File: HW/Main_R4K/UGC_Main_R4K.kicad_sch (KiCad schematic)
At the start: 165 parts, among them J1 SM02B-SURS-TF_LF__SN_, J10 SM02B-SURS-TF_LF__SN_, J13 503480-0640, J2 503480-0640, J4 Conn_01x06_Pin, J5 UJ31-CH-G1-SMT-TR, J6 Trigger, J7 Trigger, J8 Conn_01x02, J9 Conn_01x02, Q1 MMBT3904, Q2 MMBT3904, Q3 BSS138DW, Q4 BSS138DW, Q5 MMBT2222A, Q6 MMBT2222A, SW1 1TS026A-1000-0550, SW1 SW_Push, SW10 SW_Push, SW11 SW_Push, SW12 SW_Push, SW13 SW_Push, SW14 SW_TS-1187A, SW17 SW_TS-1187A, SW18 SW_TS-1187A, SW19 SW_TS-1187A, SW2 SW_Push, SW3 SW_Push, SW4 SW_Push, SW5 SW_TS-1187A, SW6 GL18_SW, SW7 SW_Push, SW8 SW_Push, SW9 SW_TS-1187A, U1 ESP32-PICO-MINI-02, U10 ST_LSM6, U11 BQ25180, U12 CH340K, U13 PI3USB4000A, U2 GD25Q80EEIGR, U4 TPS630001RCR, U5 ST_LSM6, U6 MCP3002, U7 MCP3002, U8 RP2040, X1 ModConnect, X2 ModConnect, X3 ModConnect, X4 ModConnect, X5 ModConnect, X6 ModConnect, Y1 Crystal_GND3

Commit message: Update PCB schematic
 fix diode issue
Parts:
- D14, D15, D16, D3, D6, D7: MPN B5819W SL -> B5819WT
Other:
- note added: "3.3 Regulation"
- note added: "Analog Joystick"
- note added: "I/O Buttons"
- note added: "USB I/O"
- company: (none) -> Hand Held Legend, LLC
- moved on the sheet: B1, C1, C10, C12, C13, C14, C15, C16, C17, C18, C2, C20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

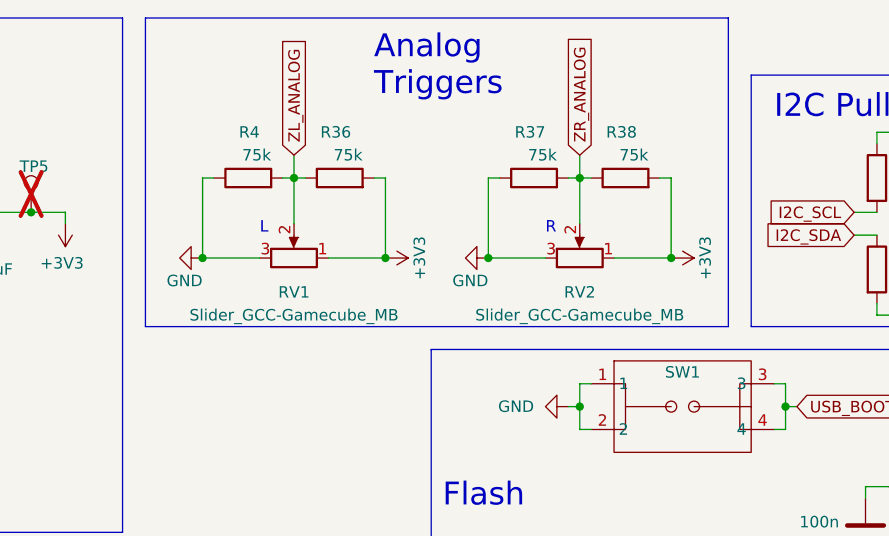
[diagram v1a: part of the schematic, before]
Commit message: Update CAD files
- PCB uses a new socket type for the slider potentiometers
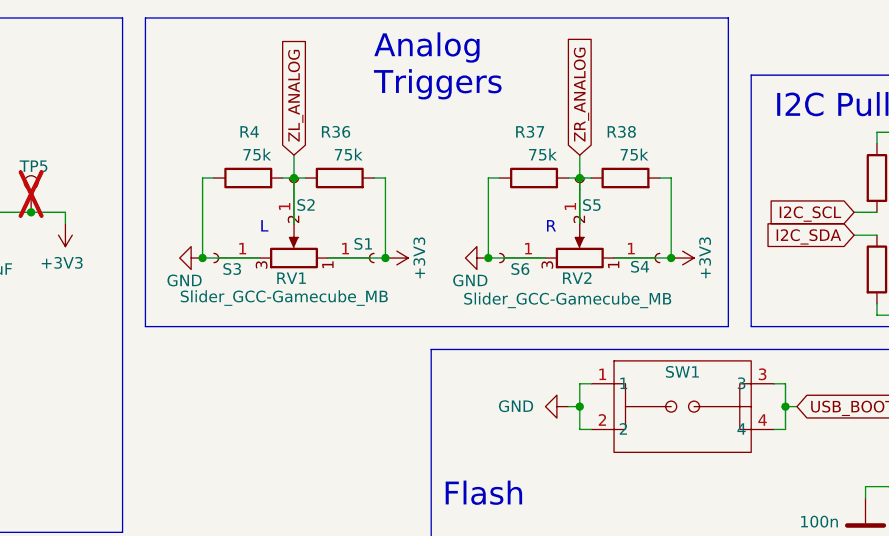
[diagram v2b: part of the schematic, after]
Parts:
- added S1, S2, S3, S4, S5, S6: 4015-0-43-80-30-27-10-0, hhl:4015-0-43-80-30-27-10-0, symbol Connector:Conn_01x01_Socket
- RV1, RV2: footprint hhl:GCC_Slider_MillMax -> hhl:GCC_Slider_MillMaxSocketed; symbol hhl:Slider_GCC-Gamecube_MillMax_MB -> hhl:Slider_GCC-Gamecube_SolderInsert
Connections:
- net +3V3: now also S1.1 (Pin_1), S4.1 (Pin_1); no longer RV1.1 (GND), RV2.1 (GND)
- net GND: now also S3.1 (Pin_1), S6.1 (Pin_1); no longer RV1.3 (V+), RV2.3 (V+)
- net ZL_ANALOG: now also S2.1 (Pin_1); no longer RV1.2 (Signal)
- net ZR_ANALOG: now also S5.1 (Pin_1); no longer RV2.2 (Signal)

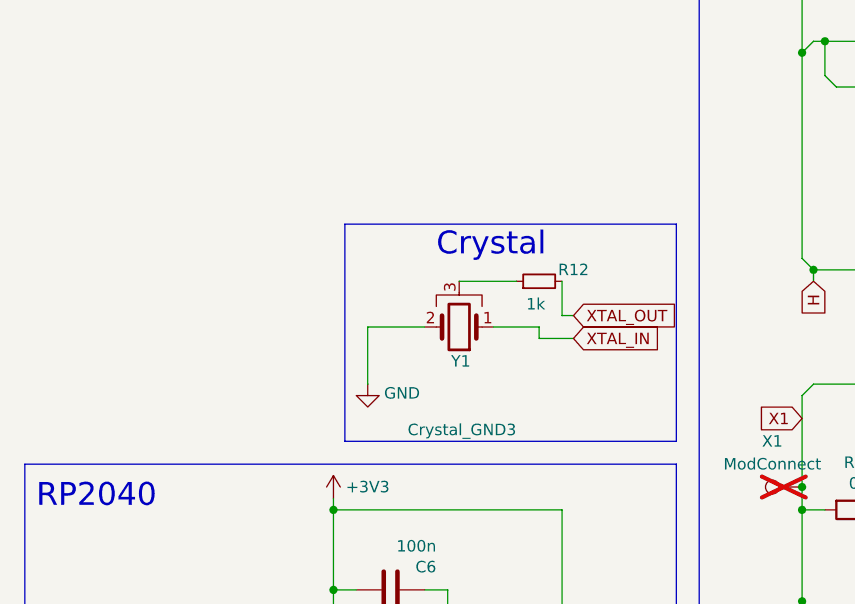
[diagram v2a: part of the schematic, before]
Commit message: Update PCBs
- New S1 variant
- Update crystal and socket mounts for trigger sliders
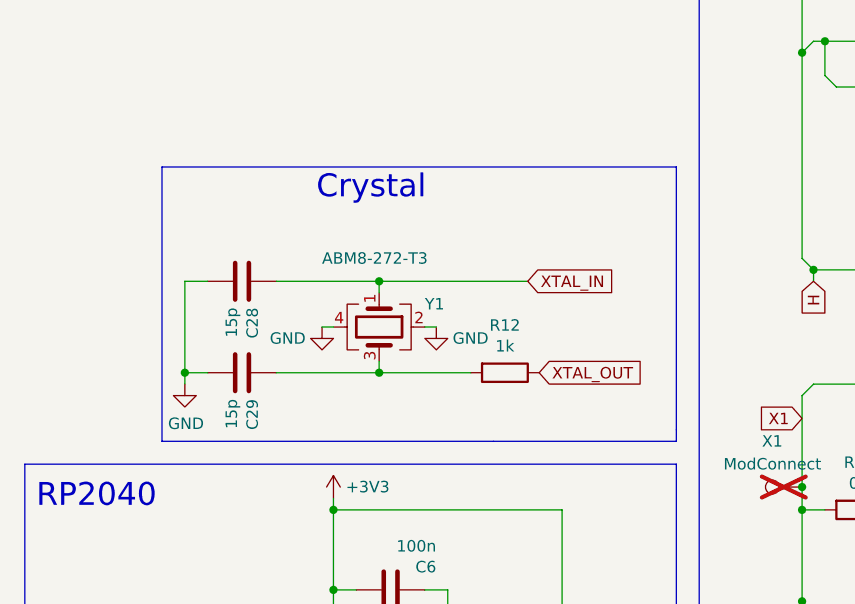
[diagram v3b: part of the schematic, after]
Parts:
- removed R12: 1k, Resistor_SMD:R_0201_0603Metric, symbol Device:R_Small
- removed Y1: Crystal_GND3, Crystal:Resonator_SMD_Murata_CSTxExxV-3Pin_3.0x1.1mm, symbol Device:Crystal_GND3
- added C28, C29: 15p, Capacitor_SMD:C_0402_1005Metric, symbol Device:C
- added R12: 1k, Resistor_SMD:R_0402_1005Metric, symbol Device:R
- added Y1: ABM8-272-T3, Crystal:Crystal_SMD_3225-4Pin_3.2x2.5mm, symbol Device:Crystal_GND24
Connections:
- net GND: now also C28.2, C29.2, Y1.2, Y1.4
- net XTAL_IN: now also C28.1, Y1.1
- net XTAL_OUT: now also R12.1
- new net: C29.1, R12.2, Y1.3

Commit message: Update PCBs
- Fix BOMs so they reference real part numbers
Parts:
- removed N1, N2, N3, N4, N5, N6: 0630-0-15-15-30-27-10-0, N/A, symbol Connector_Generic:Conn_01x01
- B1, J6, J7: LCSC (none) -> C7499302; MPN (none) -> PH2.0 mm Female; Price (none) -> 0.0098
- C1: value 47uF 6.3v -> 47uF; LCSC (none) -> C7190; MPN (none) -> TAJA476K006RNJ; Price (none) -> 0.0544
- C1, C2: value .047u -> 47nF; footprint Capacitor_SMD:C_0603_1608Metric_Pad1.08x0.95mm_HandSolder -> Capacitor_SMD:C_0603_1608Metric; LCSC C15849 -> C519554; MPN (none) -> CC0603JRX7R9BB473; Price (none) -> 0.0026
- C10, C15, C18, C20, C22, C24, C6: value 100n -> 100nF; LCSC (none) -> C160831; MPN (none) -> CL03A104KQ3NNNC; Price (none) -> 0.0007
- C10, C5, C7, C9: value 100n -> 100nF; footprint Capacitor_SMD:C_0402_1005Metric -> Capacitor_SMD:C_0201_0603Metric; LCSC (none) -> C160831; MPN (none) -> CL03A104KQ3NNNC; Price (none) -> 0.0007
- C12, C13: footprint Capacitor_SMD:C_0603_1608Metric -> Capacitor_SMD:C_0201_0603Metric; LCSC C1525 -> C160831; MPN (none) -> CL03A104KQ3NNNC; Price (none) -> 0.0007
- C14, C16, C21, C26, C27, C33, C34: value 1u -> 1uF; LCSC (none) -> C76929; MPN (none) -> GRM033R60J105KEA2D; Price (none) -> 0.0015
- C17: footprint Capacitor_SMD:C_0402_1005Metric -> Capacitor_SMD:C_0805_2012Metric; LCSC (none) -> C17024; MPN (none) -> CL21A106KPFNNNE; Price (none) -> 0.0050
- C2, C3: LCSC (none) -> C17024; MPN (none) -> CL21A106KPFNNNE; Price (none) -> 0.0050
- C2: value 10uF/10V (20%) -> 10uF; footprint Capacitor_SMD:C_0603_1608Metric -> Capacitor_SMD:C_0805_2012Metric; LCSC (none) -> C17024; MPN (none) -> CL21A106KPFNNNE; Price (none) -> 0.0050
- C25, C32: LCSC (none) -> C160831; MPN (none) -> CL03A104KQ3NNNC; Price (none) -> 0.0007
- C28, C29: value 15p -> 15pF; LCSC (none) -> C85891; MPN (none) -> GRM0335C1H150JA01D; Price (none) -> 0.0011
- C8: value 1u -> 1uF; footprint Capacitor_SMD:C_0402_1005Metric -> Capacitor_SMD:C_0201_0603Metric; LCSC (none) -> C76929; MPN (none) -> GRM033R60J105KEA2D; Price (none) -> 0.0015
- D1, D10, D9: LCSC (none) -> C27636112; Price 0.0449 -> 0.0092
- D1, D11, D12, D13, D2, D8: LCSC (none) -> C135826; MPN (none) -> BAS16VY,115
- J1, J10: LCSC (none) -> C566239
- J13, J2: LCSC (none) -> C3168077
- J4, J8, J9, JP1, SW1, SW10, SW11, SW12, SW13, SW2, SW3, SW4, TP1, TP2, TP5, TP6, TP7, X1, X2, X3, X4, X5, X6: MPN (none) -> N/A
- J5: LCSC (none) -> C22359729
- L1, L10, L11, L12, L13, L2, L3, L4, L6: LCSC (none) -> C2890035; Price 0.0506 -> 0.0492
- Q1, Q2: LCSC (none) -> C2891808; Price 0.0048 -> 0.0035
- Q5, Q6: LCSC (none) -> C916372; MPN (none) -> MMBT2222A
- R1, R2, R23, R24, R25, R26, R27, R28, R7, R8, R9: LCSC (none) -> C138165; MPN (none) -> RC0201FR-071KL; Price (none) -> 0.0006
- R11: value 330 -> 330R; footprint Resistor_SMD:R_0402_1005Metric -> Resistor_SMD:R_0201_0603Metric; LCSC (none) -> C274872; MPN (none) -> RC0201FR-07330RL; Price (none) -> 0.0006
- R12: footprint Resistor_SMD:R_0402_1005Metric -> Resistor_SMD:R_0201_0603Metric; LCSC (none) -> C138165; MPN (none) -> RC0201FR-071KL; Price (none) -> 0.0006
- R13, R14, R36, R37, R38, R4: footprint Resistor_SMD:R_0603_1608Metric -> Resistor_SMD:R_0201_0603Metric; LCSC (none) -> C2107901; MPN (none) -> AF0201FR-0775KL; Price (none) -> 0.0006
- R15, R16, R17, R20, R29, R30, R5: LCSC (none) -> C106225; MPN (none) -> RC0201FR-0710KL; Price (none) -> 0.0006
- R18, R19: value 0 -> 0R; LCSC (none) -> C106227; MPN (none) -> RC0201FR-070RL; Price (none) -> 0.0006
- R21, R22: value 5.1kohm -> 5.1k; footprint Resistor_SMD:R_0603_1608Metric -> Resistor_SMD:R_0201_0603Metric; LCSC (none) -> C274341; MPN (none) -> RC0201FR-075K1L; Price (none) -> 0.0004
- R3: value 100 -> 100R; LCSC (none) -> C77623; MPN (none) -> RC0201FR-07100RL; Price (none) -> 0.0006
- R31, R39: footprint Resistor_SMD:R_0402_1005Metric -> Resistor_SMD:R_0201_0603Metric; LCSC C25804 -> C106225; MPN (none) -> RC0201FR-0710KL; Price (none) -> 0.0006
- R32, R40: footprint Resistor_SMD:R_0402_1005Metric -> Resistor_SMD:R_0201_0603Metric; LCSC C22775 -> C77623; MPN (none) -> RC0201FR-07100RL; Price (none) -> 0.0006
- R33, R41: footprint Resistor_SMD:R_0402_1005Metric -> Resistor_SMD:R_0201_0603Metric; LCSC C22775 -> C106227; MPN (none) -> RC0201FR-070RL; Price (none) -> 0.0006
- R34, R35: footprint Resistor_SMD:R_0402_1005Metric -> Resistor_SMD:R_0201_0603Metric; LCSC (none) -> C106227; MPN (none) -> RC0201FR-070RL; Price (none) -> 0.0006
- R6, R7: value 27 -> 27R; LCSC (none) -> C490808; MPN (none) -> ERA1AEB103C; Price (none) -> 0.0523
- RV1, RV2: LCSC (none) -> C127475
- S1, S2, S3, S4, S5, S6: LCSC (none) -> C17526581; Price (none) -> 0.754
- U1: LCSC (none) -> C2980306
- U4: LCSC (none) -> C28060
- U6, U7: LCSC (none) -> C635958
- U8: LCSC (none) -> C2040
- Y1: LCSC (none) -> C20625731; Price (none) -> 0.2381

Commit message: Fix some wrong MPNs
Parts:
- C28, C29: LCSC C85891 -> C326803; MPN GRM0335C1H150JA01D -> CC0402FRNPO9BN150; Price 0.0011 -> 0.0022
- R18, R19, R33, R34, R35, R41: Price 0.0006 -> 0.0005
- R6, R7: LCSC C490808 -> C273268; MPN ERA1AEB103C -> RC0201FR-0727RL; Price 0.0523 -> 0.0006
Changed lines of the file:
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@@
 			)
 		)
-		(property "Price" "0.0006"
+		(property "Price" "0.0005"
 			(at 156.21 133.35 0)
 			(effects
@@
 			)
 		)
-		(property "Price" "0.0006"
+		(property "Price" "0.0005"
 			(at 156.21 129.54 0)
 			(effects
@@
 			)
 		)
-		(property "Price" "0.0006"
+		(property "Price" "0.0005"
 			(at 424.18 234.95 0)
 			(effects
@@
 			)
 		)
-		(property "LCSC" "C85891"
+		(property "LCSC" "C326803"
 			(at 325.12 212.09 0)
 			(effects
@@
 			)
 		)
-		(property "MPN" "GRM0335C1H150JA01D"
+		(property "MPN" "CC0402FRNPO9BN150"
 			(at 325.12 212.09 0)
 			(effects
@@
 			)
 		)
-		(property "Price" "0.0011"
+		(property "Price" "0.0022"
 			(at 325.12 212.09 0)
 			(effects
@@
 			)
 		)
-		(property "LCSC" "C490808"
+		(property "LCSC" "C273268"
 			(at 294.64 288.29 0)
 			(effects
@@
 			)
 		)
-		(property "MPN" "ERA1AEB103C"
+		(property "MPN" "RC0201FR-0727RL "
 			(at 294.64 288.29 0)
 			(effects
@@
 			)
 		)
-		(property "Price" "0.0523"
+		(property "Price" "0.0006"
 			(at 294.64 288.29 0)
 			(effects
@@
 			)
 		)
-		(property "Price" "0.0006"
+		(property "Price" "0.0005"
 			(at 224.79 331.47 0)
 			(effects
@@
 			)
 		)
-		(property "LCSC" "C490808"
+		(property "LCSC" "C273268"
 			(at 294.64 285.75 0)
 			(effects
@@
 			)
 		)
-		(property "MPN" "ERA1AEB103C"
+		(property "MPN" "RC0201FR-0727RL "
 			(at 294.64 285.75 0)
 			(effects
@@
 			)
 		)
-		(property "Price" "0.0523"
+		(property "Price" "0.0006"
 			(at 294.64 285.75 0)
 			(effects
@@
 			)
 		)
-		(property "Price" "0.0006"
+		(property "Price" "0.0005"
 			(at 393.7 237.49 0)
 			(effects
@@
 			)
 		)
-		(property "Price" "0.0006"
+		(property "Price" "0.0005"
 			(at 224.79 276.86 0)
 			(effects
@@
 			)
 		)
-		(property "LCSC" "C85891"
+		(property "LCSC" "C326803"
 			(at 325.12 222.25 0)
 			(effects
@@
 			)
 		)
-		(property "MPN" "GRM0335C1H150JA01D"
+		(property "MPN" "CC0402FRNPO9BN150"
 			(at 325.12 222.25 0)
 			(effects
@@
 			)
 		)
-		(property "Price" "0.0011"
+		(property "Price" "0.0022"
 			(at 325.12 222.25 0)
 			(effects

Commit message: Minor updates to text
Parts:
- B1, J6, J7: Confirmed (none) -> YES; LCSC C7499302 -> C5175230; MPN PH2.0 mm Female -> HDGC2001WV-2P
- C1, C10, C12, C13, C14, C15, C16, C17, C18, C2, C20, C21, C22, C24, C25, C26, C27, C28, C29, C3, C32, C33, C34, C5, C6, C7, C8, C9, D1, D10, D11, D12, D13, D14, D15, D16, D2, D3, D6, D7, D8, D9, J1, J10, J13, J2, J5, L1, L10, L11, L12, L13, L2, L3, L4, L5, L6, Q1, Q2, Q3, Q4, Q5, Q6, R1, R11, R12, R13, R14, R15, R16, R17, R18, R19, R2, R20, R21, R22, R23, R24, R25, R26, R27, R28, R29, R3, R30, R31, R32, R33, R34, R35, R36, R37, R38, R39, R4, R40, R41, R5, R6, R7, R8, R9, RV1, RV2, S1, S2, S3, S4, S5, S6, SW1, U1, U10, U5: Confirmed (none) -> YES
- SW14, SW17, SW18, SW19, SW5, SW9: Confirmed (none) -> YES; LCSC (none) -> C480267

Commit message: PCB Production files update
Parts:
- B1, J6, J7: Link (none) -> https://www.lcsc.com/product-detail/Wire-To-Board-Connector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; Package (none) -> Plugin,P=2mm
- C1: Link (none) -> https://www.lcsc.com/product-detail/Tantalum-Capacitors_Kyo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; Package (none) -> CASE-A-3216-18(mm)
- C1, C2: Link (none) -> https://www.lcsc.com/product-detail/Multilayer-Ceramic-Capa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; Package (none) -> 0603
- C10, C12, C13, C14, C15, C16, C18, C20, C21, C22, C24, C25, C26, C27, C32, C33, C34, C5, C6, C7, C8, C9: Link (none) -> https://www.lcsc.com/product-detail/Multilayer-Ceramic-Capa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; Package (none) -> 0201
- C17, C2, C3: Link (none) -> https://www.lcsc.com/product-detail/Multilayer-Ceramic-Capa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; Package (none) -> 0805
- C28, C29: Link (none) -> https://www.lcsc.com/product-detail/Multilayer-Ceramic-Capa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; Package (none) -> 0402
- D1, D10, D9: Link (none) -> https://www.lcsc.com/product-detail/Schottky-Diodes_DOWO-CU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; Package (none) -> SOD-323
- D1, D11, D12, D13, D2, D8: Link (none) -> https://www.lcsc.com/product-detail/Diodes-General-Purpose_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; Package (none) -> SOT-363
- D14, D15, D16, D3, D6, D7: Link (none) -> https://www.lcsc.com/product-detail/Schottky-Diodes_LGE-B58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; Package (none) -> SOD-523
- J1, J10: Link (none) -> https://www.lcsc.com/product-detail/Wire-To-Board-Connector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; Package None -> SMD,P=0.8mm,Surface Mount，Right Angle
- J13, J2: Link (none) -> https://www.lcsc.com/product-detail/FFC-FPC-Flat-Flexible-C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; MPN 503480-0640 -> 5034800640; Package (none) -> SMD,P=0.5mm,Surface Mount，Right Angle
- J5: Link (none) -> https://www.lcsc.com/product-detail/USB-Connectors_CUI-UJ31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; Package None -> -
- L1, L10, L11, L12, L13, L2, L3, L4, L6: Link (none) -> https://www.lcsc.com/product-detail/RGB-LEDs-Built-in-IC_OP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; Package (none) -> 0606
- L5: Link (none) -> https://www.lcsc.com/product-detail/Inductors-SMD_INPAQ-MIP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; Package (none) -> 1008
- Q1, Q2: Link (none) -> https://www.lcsc.com/product-detail/Bipolar-BJT_YONGYUTAI-M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; Package (none) -> SOT-23
- Q3, Q4: Link (none) -> https://www.lcsc.com/product-detail/MOSFETs_Diodes-Incorpor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; Package (none) -> SC-70-6(SOT-363)
- Q5, Q6: Link (none) -> https://www.lcsc.com/product-detail/Bipolar-BJT_JSMSEMI-MMB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; Package (none) -> SOT-23
- R1, R11, R12, R13, R14, R15, R16, R17, R18, R19, R2, R20, R21, R22, R23, R24, R25, R26, R27, R28, R29, R3, R30, R31, R32, R33, R34, R35, R36, R37, R38, R39, R4, R40, R41, R5, R6, R7, R8, R9: Link (none) -> https://www.lcsc.com/product-detail/Chip-Resistor-Surface-M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; Package (none) -> 0201
- RV1, RV2: LCSC C127475 -> -; Link (none) -> -; Package (none) -> -; now not fitted
- S1, S2, S3, S4, S5, S6: Link (none) -> https://www.lcsc.com/product-detail/Connector-Accessories_M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; Package (none) -> -
- SW1: Link (none) -> https://www.lcsc.com/product-detail/Tactile-Switches_HYP-Ho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; Package (none) -> SMD,1.6x2.6mm
- SW14, SW17, SW18, SW19, SW5, SW9: value SW_TS-1187A -> TS-1187A-C-A-B; Link (none) -> https://www.lcsc.com/product-detail/Tactile-Switches_XKB-Co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; Package (none) -> SMD
- SW7, SW8: LCSC (none) -> -; Link (none) -> -; Package (none) -> -
- U1: Link (none) -> https://www.lcsc.com/product-detail/WiFi-Modules_Espressif-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; Package (none) -> -
- U10, U5: Link (none) -> https://www.lcsc.com/product-detail/Accelerometers_STMicroe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; Package (none) -> LGA-14(2.5x3)
- U11: Link (none) -> https://www.lcsc.com/product-detail/Battery-Management_Texa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; Package (none) -> DSBGA-8(1.1x1.6)
- U12: Link (none) -> https://www.lcsc.com/product-detail/USB-Converters_WCH-Jian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; Package (none) -> ESSOP-10-150mil-1mm
- U13: Link (none) -> https://www.lcsc.com/product-detail/Analog-Switches-Multipl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; Package (none) -> UQFN-10(1.5x2)
- U2: Link (none) -> https://www.lcsc.com/product-detail/NOR-FLASH_GigaDevice-Se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; Package (none) -> USON-8-EP(2x3)
- U4: Link (none) -> https://www.lcsc.com/product-detail/DC-DC-Converters_Texas-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
- U6, U7: Link (none) -> https://www.lcsc.com/product-detail/Analog-to-Digital-Conve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; Package (none) -> MSOP-8
- U8: Link (none) -> https://www.lcsc.com/product-detail/Microcontrollers-MCU-MP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; Package (none) -> LQFN-56(7x7)
- Y1: Link (none) -> https://www.lcsc.com/product-detail/Crystals_Abracon-LLC-AB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; Package (none) -> SMD3225-4P

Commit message: Update BOM for diode
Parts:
- D1, D10, D9: value CUS08F30 -> CUS08F30,H3F; LCSC C27636112 -> C150183; Link https://www.lcsc.com/product-detail/Schottky-Diodes_DOWO-CU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 -> https://www.lcsc.com/product-detail/Schottky-Diodes_TOSHIBA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; MPN CUS08F30 -> CUS08F30,H3F
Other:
- note added: "Crystal Oscillator"
- note added: "Frequency: 12MHz Load capacitance: 10pF Tolerance: 30PPM ESR: 50 Ohms Drive Level: 10 uW"
- note removed: "Crystal"
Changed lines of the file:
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@@
 	(polyline
 		(pts
-			(xy 373.38 199.39) (xy 373.38 228.6)
+			(xy 373.38 185.42) (xy 373.38 228.6)
 		)
 		(stroke
@@
 	(polyline
 		(pts
-			(xy 353.06 229.87) (xy 316.23 229.87)
+			(xy 353.06 229.87) (xy 300.99 229.87)
 		)
 		(stroke
@@
 	(polyline
 		(pts
-			(xy 316.23 199.39) (xy 316.23 229.87)
+			(xy 300.99 185.42) (xy 300.99 229.87)
 		)
 		(stroke
@@
 	(polyline
 		(pts
-			(xy 316.23 199.39) (xy 373.38 199.39)
+			(xy 300.99 185.42) (xy 373.38 185.42)
 		)
 		(stroke
@@
 		)
 	)
+	(text "Frequency: 12MHz\nLoad capacitance: 10pF\nTolerance: 30PPM\nESR: 50 Ohms\nDrive Level: 10 uW"
+		(exclude_from_sim no)
+		(at 302.006 205.74 0)
+		(effects
+			(font
+				(size 2 2)
+			)
+			(justify left bottom)
+		)
+	)
 	(text "B"
 		(exclude_from_sim no)
@@
 		)
 	)
-	(text "Crystal"
+	(text "Crystal Oscillator"
 		(exclude_from_sim no)
-		(at 333.375 203.2 0)
+		(at 301.752 189.738 0)
 		(effects
 			(font
@@
 			)
 		)
-		(property "Value" "CUS08F30"
-			(at 248.92 215.9 0)
+		(property "Value" "CUS08F30,H3F"
+			(at 244.094 215.9 0)
 			(effects
 				(font
@@
 			)
 		)
-		(property "MPN" "CUS08F30"
+		(property "MPN" "CUS08F30,H3F"
 			(at 248.92 218.44 0)
 			(effects
@@
 			)
 		)
-		(property "LCSC" "C27636112"
+		(property "LCSC" "C150183"
 			(at 248.92 218.44 0)
 			(effects
@@
 			)
 		)
-		(property "Link" "https://www.lcsc.com/product-detail/Schottky-Diodes_DOWO-CUS08F30_C27636112.html"
+		(property "Link" "https://www.lcsc.com/product-detail/Schottky-Diodes_TOSHIBA-CUS08F30-H3F_C150183.html?s_z=n_C150183"
 			(at 248.92 218.44 0)
 			(effects
@@
 			)
 		)
-		(property "Value" "CUS08F30"
-			(at 234.95 245.11 0)
+		(property "Value" "CUS08F30,H3F"
+			(at 239.014 244.856 0)
 			(effects
 				(font
@@
 			)
 		)
-		(property "MPN" "CUS08F30"
+		(property "MPN" "CUS08F30,H3F"
 			(at 234.95 247.65 0)
 			(effects
@@
 			)
 		)
-		(property "LCSC" "C27636112"
+		(property "LCSC" "C150183"
 			(at 234.95 247.65 0)
 			(effects
@@
 			)
 		)
-		(property "Link" "https://www.lcsc.com/product-detail/Schottky-Diodes_DOWO-CUS08F30_C27636112.html"
+		(property "Link" "https://www.lcsc.com/product-detail/Schottky-Diodes_TOSHIBA-CUS08F30-H3F_C150183.html?s_z=n_C150183"
 			(at 234.95 247.65 0)
 			(effects
@@
 		(dnp no)
 		(property "Reference" "R13"
-			(at 195.58 248.92 90)
+			(at 193.04 251.46 90)
 			(effects
 				(font
@@
 			)
 		)
-		(property "Value" "CUS08F30"
+		(property "Value" "CUS08F30,H3F"
 			(at 273.05 62.23 0)
 			(effects
@@
 			)
 		)
-		(property "MPN" "CUS08F30"
+		(property "MPN" "CUS08F30,H3F"
 			(at 270.51 62.23 0)
 			(effects
@@
 			)
 		)
-		(property "LCSC" "C27636112"
+		(property "LCSC" "C150183"
 			(at 270.51 62.23 0)
 			(effects
@@
 			)
 		)
-		(property "Link" "https://www.lcsc.com/product-detail/Schottky-Diodes_DOWO-CUS08F30_C27636112.html"
+		(property "Link" "https://www.lcsc.com/product-detail/Schottky-Diodes_TOSHIBA-CUS08F30-H3F_C150183.html?s_z=n_C150183"
 			(at 270.51 62.23 0)
 			(effects
@@
 			)
 		)
-		(property "Value" "CUS08F30"
+		(property "Value" "CUS08F30,H3F"
 			(at 318.77 57.15 0)
 			(effects
@@
 			)
 		)
-		(property "MPN" "CUS08F30"
+		(property "MPN" "CUS08F30,H3F"
 			(at 318.77 59.69 0)
 			(effects
@@
 			)
 		)
-		(property "LCSC" "C27636112"
+		(property "LCSC" "C150183"
 			(at 318.77 59.69 0)
 			(effects
@@
 			)
 		)
-		(property "Link" "https://www.lcsc.com/product-detail/Schottky-Diodes_DOWO-CUS08F30_C27636112.html"
+		(property "Link" "https://www.lcsc.com/product-detail/Schottky-Diodes_TOSHIBA-CUS08F30-H3F_C150183.html?s_z=n_C150183"
 			(at 318.77 59.69 0)
 			(effects
